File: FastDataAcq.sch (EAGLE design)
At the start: 229 parts, among them IC1 LT1963AEQ, IC2 FT230XQ, IC3 ADCMP553BRMZ, J1 USB_MICROAB_SMT, J2 MICRO-FIT_3.0_2POS_RA_SMD, X1 SMA-142-0701-801/806, X2 87832-14, X3 SMA-142-0701-801/806, Y1 SI530-500, Y2 DNP, Y3 100MHz

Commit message: Schematic fixes and beginning board layout
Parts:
- removed C105, C106, C107, C108, C109, C110, C111, C112: .1uF, Schuyler:CAPACITOR0204_REVERSE
- removed R40: 100 0.1%, rcl:R-US_R0402
- removed R41: 330, rcl:R-US_R0201
- added C16: .1uF, Schuyler:CAPACITOR0204_REVERSE
- added C66: 10pF, rcl:C-EUC0201
- added C67: 33uF, SparkFun-Passives:CAP0805
- added C69, C73: 22uF 150mOhm ESR, rcl:C-USC0805
- added C70, C72: 10uF, rcl:C-EUC0603
- added C75: NA, rcl:C-EUC0603
- C10, C11, C28, C29, C87: value 33uF -> .1uF; device SparkFun-Passives:CAP0805 -> Schuyler:CAPACITOR0204_REVERSE; PARTNUMBER 445-8238-1-ND -> 587-2152-1-ND; SUPPLIER (none) -> DIGIKEY
- C100: value .1uF -> 47pF; device Schuyler:CAPACITOR0204_REVERSE -> rcl:C-EUC0201; PARTNUMBER 587-2152-1-ND -> 445-1782-1-ND; SUPPLIER DIGIKEY -> (none)
- C101, C103: value .1uF -> 10nF; device Schuyler:CAPACITOR0204_REVERSE -> rcl:C-EUC0201; PARTNUMBER 587-2152-1-ND -> 445-1793-1-ND; SUPPLIER DIGIKEY -> (none)
- C102: value 4.7uF -> 1uF; device Schuyler:CAPACITOR0304_REVERSE -> Schuyler:CAPACITOR0204_REVERSE; PARTNUMBER 445-13745-1-ND -> 445-9091-1-ND
- C12, C13, C15, C17, C22: value 10uF -> .1uF; device rcl:C-EUC0603 -> Schuyler:CAPACITOR0204_REVERSE; PARTNUMBER 445-4112-1-ND -> 587-2152-1-ND
- C14, C25, C26, C27, C8, C9: value 10pF -> .1uF; device rcl:C-EUC0201 -> Schuyler:CAPACITOR0204_REVERSE; PARTNUMBER 445-1769-1-ND -> 587-2152-1-ND; SUPPLIER (none) -> DIGIKEY
- C18: value NA -> 10uF; PARTNUMBER (none) -> 445-4112-1-ND; SUPPLIER (none) -> DIGIKEY
- C2: value 10uF -> 10pF; device rcl:C-EUC0603 -> rcl:C-EUC0201; PARTNUMBER 445-4112-1-ND -> 445-1769-1-ND; SUPPLIER DIGIKEY -> (none)
- C20: value 10uF -> 100uF; device rcl:C-EUC0603 -> Schuyler:CAP_POL_D9_SERIES; MANPARTNUMBER (none) -> ECASD91B107M012K00; PARTNUMBER 445-4112-1-ND -> 490-5480-1-ND; SUPPLIER DIGIKEY -> (none)
- C23, C24: value 22uF 150mOhm ESR -> .1uF; device rcl:C-USC0805 -> Schuyler:CAPACITOR0204_REVERSE; PARTNUMBER P16231CT-ND -> 587-2152-1-ND
- C3: value 100uF -> 33uF; device Schuyler:CAP_POL_D9_SERIES -> SparkFun-Passives:CAP0805; MANPARTNUMBER ECASD91B107M012K00 -> (none); PARTNUMBER 490-5480-1-ND -> 445-8238-1-ND
- C30, C38: value 33uF -> 0.47uF; device SparkFun-Passives:CAP0805 -> Schuyler:CAPACITOR0204_REVERSE; PARTNUMBER 445-8238-1-ND -> 1276-1779-1-ND; SUPPLIER (none) -> DIGIKEY
- C31: value 22uF 150mOhm ESR -> 33uF; device rcl:C-USC0805 -> SparkFun-Passives:CAP0805; PARTNUMBER P16231CT-ND -> 445-8238-1-ND; SUPPLIER DIGIKEY -> (none)
- C32, C65, C68: value 4.7uF -> 10uF; device Schuyler:CAPACITOR0304_REVERSE -> rcl:C-EUC0603; PARTNUMBER 445-13745-1-ND -> 445-4112-1-ND
- C33, C71: value 4.7uF -> 10pF; device Schuyler:CAPACITOR0304_REVERSE -> rcl:C-EUC0201; PARTNUMBER 445-13745-1-ND -> 445-1769-1-ND; SUPPLIER DIGIKEY -> (none)
- C34, C74: value 4.7uF -> 33uF; device Schuyler:CAPACITOR0304_REVERSE -> SparkFun-Passives:CAP0805; PARTNUMBER 445-13745-1-ND -> 445-8238-1-ND; SUPPLIER DIGIKEY -> (none)
- C35, C40, C50: device Schuyler:CAPACITOR0304_REVERSE -> Schuyler:CAPACITOR; PARTNUMBER 445-13745-1-ND -> (none); SUPPLIER DIGIKEY -> (none)
- C36, C37, C41, C42, C45, C62: value 0.47uF -> 4.7uF; device Schuyler:CAPACITOR0304_REVERSE -> Schuyler:CAPACITOR; PARTNUMBER 445-13744-1-ND -> (none); SUPPLIER DIGIKEY -> (none)
- C39: value 33uF -> 4.7uF; device SparkFun-Passives:CAP0805 -> Schuyler:CAPACITOR; PARTNUMBER 445-8238-1-ND -> (none)
- C43, C44, C47, C93: value .1uF -> 4.7uF; device Schuyler:CAPACITOR0204_REVERSE -> Schuyler:CAPACITOR; PARTNUMBER 587-2152-1-ND -> (none); SUPPLIER DIGIKEY -> (none)
- C46, C48, C49: value .1uF -> 0.47uF; PARTNUMBER 587-2152-1-ND -> 1276-1779-1-ND
- C5: value NA -> 10pF; device rcl:C-EUC0603 -> rcl:C-EUC0201; PARTNUMBER (none) -> 445-1769-1-ND
- C51, C52, C60: value 4.7uF -> 0.47uF; device Schuyler:CAPACITOR0304_REVERSE -> Schuyler:CAPACITOR0204_REVERSE; PARTNUMBER 445-13745-1-ND -> 1276-1779-1-ND
- C53, C58: value .1uF -> 10uF; device Schuyler:CAPACITOR0204_REVERSE -> rcl:C-EUC0603; PARTNUMBER 587-2152-1-ND -> 445-4112-1-ND
- C54: value .1uF -> 10pF; device Schuyler:CAPACITOR0204_REVERSE -> rcl:C-EUC0201; PARTNUMBER 587-2152-1-ND -> 445-1769-1-ND; SUPPLIER DIGIKEY -> (none)
- C55: value 0.47uF -> 33uF; device Schuyler:CAPACITOR0304_REVERSE -> SparkFun-Passives:CAP0805; PARTNUMBER 445-13744-1-ND -> 445-8238-1-ND; SUPPLIER DIGIKEY -> (none)
- C56: value 0.47uF -> 10uF; device Schuyler:CAPACITOR0304_REVERSE -> rcl:C-EUC0603; PARTNUMBER 445-13744-1-ND -> 445-4112-1-ND
- C57: value 4.7uF -> 22uF 150mOhm ESR; device Schuyler:CAPACITOR0304_REVERSE -> rcl:C-USC0805; PARTNUMBER 445-13745-1-ND -> P16231CT-ND
- C59: value 10nF -> 4.7uF; device rcl:C-EUC0201 -> Schuyler:CAPACITOR; PARTNUMBER 445-1793-1-ND -> (none)
- C6: value 10uF -> 33uF; device rcl:C-EUC0603 -> SparkFun-Passives:CAP0805; PARTNUMBER 445-4112-1-ND -> 445-8238-1-ND; SUPPLIER DIGIKEY -> (none)
- C61: device Schuyler:CAPACITOR0304_REVERSE -> Schuyler:CAPACITOR0204_REVERSE; PARTNUMBER 445-13744-1-ND -> 1276-1779-1-ND
- C63: value 1uF -> 0.47uF; PARTNUMBER 445-9091-1-ND -> 1276-1779-1-ND
- C64: value 10nF -> 0.47uF; device rcl:C-EUC0201 -> Schuyler:CAPACITOR0204_REVERSE; PARTNUMBER 445-1793-1-ND -> 1276-1779-1-ND; SUPPLIER (none) -> DIGIKEY
- C7: value 10uF -> NA; PARTNUMBER 445-4112-1-ND -> (none); SUPPLIER DIGIKEY -> (none)
- C76: value 0.47uF -> 10nF; device Schuyler:CAPACITOR0304_REVERSE -> rcl:C-EUC0201; PARTNUMBER 445-13744-1-ND -> 445-1793-1-ND; SUPPLIER DIGIKEY -> (none)
- C77: value 100pF -> .1uF; device rcl:C-EUC0603 -> Schuyler:CAPACITOR0204_REVERSE; PARTNUMBER 1276-1295-1-ND -> 587-2152-1-ND
- C78: value .1uF -> 1uF; PARTNUMBER 587-2152-1-ND -> 445-9091-1-ND
- C79, C82: value .1uF -> 4.7nF; device Schuyler:CAPACITOR0204_REVERSE -> rcl:C-EUC0201; PARTNUMBER 587-2152-1-ND -> 445-1795-1-ND; SUPPLIER DIGIKEY -> (none)
- C80: value 4.7nF -> .1uF; device rcl:C-EUC0201 -> Schuyler:CAPACITOR0204_REVERSE; PARTNUMBER 445-1795-1-ND -> 587-2152-1-ND; SUPPLIER (none) -> DIGIKEY
- C81: value 4.7nF -> 1uF; device rcl:C-EUC0201 -> Schuyler:CAPACITOR0204_REVERSE; PARTNUMBER 445-1795-1-ND -> 445-9091-1-ND; SUPPLIER (none) -> DIGIKEY
- C84: value 33uF -> 10nF; device SparkFun-Passives:CAP0805 -> rcl:C-EUC0201; PARTNUMBER 445-8238-1-ND -> 445-1793-1-ND
- C86: value 1uF -> 10nF; device Schuyler:CAPACITOR0204_REVERSE -> rcl:C-EUC0201; PARTNUMBER 445-9091-1-ND -> 445-1793-1-ND; SUPPLIER DIGIKEY -> (none)
- C88: value 4.7uF -> 100pF; device Schuyler:CAPACITOR0304_REVERSE -> rcl:C-EUC0201; PARTNUMBER 445-13745-1-ND -> 445-4675-1-ND
- C90, C94: value 10nF -> .1uF; device rcl:C-EUC0201 -> Schuyler:CAPACITOR0204_REVERSE; PARTNUMBER 445-1793-1-ND -> 587-2152-1-ND; SUPPLIER (none) -> DIGIKEY
- C91: value .1uF -> 33uF; device Schuyler:CAPACITOR0204_REVERSE -> SparkFun-Passives:CAP0805; PARTNUMBER 587-2152-1-ND -> 445-8238-1-ND; SUPPLIER DIGIKEY -> (none)
- C92: value 10nF -> 4.7uF; device rcl:C-EUC0201 -> Schuyler:CAPACITOR0304_REVERSE; PARTNUMBER 445-1793-1-ND -> 445-13745-1-ND; SUPPLIER (none) -> DIGIKEY
- C96: value 47pF -> .1uF; device rcl:C-EUC0201 -> Schuyler:CAPACITOR0204_REVERSE; PARTNUMBER 445-1782-1-ND -> 587-2152-1-ND; SUPPLIER (none) -> DIGIKEY
- C98: value 47pF -> 33uF; device rcl:C-EUC0201 -> SparkFun-Passives:CAP0805; PARTNUMBER 445-1782-1-ND -> 445-8238-1-ND
- C99: value 1uF -> 47pF; device Schuyler:CAPACITOR0204_REVERSE -> rcl:C-EUC0201; PARTNUMBER 445-9091-1-ND -> 445-1782-1-ND; SUPPLIER DIGIKEY -> (none)
- D2: device Schuyler:LED_0603_GREEN -> Schuyler:LED_0603_BLUE
- D3: device Schuyler:LED_0603_BLUE -> Schuyler:LED_0603_GREEN
- D4: device Schuyler:LED_0603_BLUE -> Schuyler:LED_0603_RED
- D6: device Schuyler:LED_0603_RED -> Schuyler:LED_0603_BLUE
- J1: value USB_MICROAB_SMT -> MICRO-FIT_3.0_2POS_RA_SMD; device Schuyler:USB_MICROAB_SMT -> Schuyler:MICRO-FIT_3.0_2POS_RA_SMD
- J2: value MICRO-FIT_3.0_2POS_RA_SMD -> USB_MICROAB_SMT; device Schuyler:MICRO-FIT_3.0_2POS_RA_SMD -> Schuyler:USB_MICROAB_SMT
- JP2: value M10" -> (none); device SparkFun-Connectors:M10" -> SparkFun-Passives:JUMPER-2PTH
- JP3: value (none) -> M10"; device SparkFun-Passives:JUMPER-2PTH -> SparkFun-Connectors:M10"
- L10, L7, L9: value (none) -> 2.2uH; device Schuyler:FERRITE_BEADS_BLM18SG260 -> Schuyler:INDUCTOR_3X3.6; PARTNUMBER (none) -> 541-1322-1-ND; SUPPLIER (none) -> DIGIKEY
- L11: device Schuyler:FERRITE_BEADS_BLM18SG331 -> Schuyler:FERRITE_BEADS_BLM18SG260
- L12: value CHOKE_CM_ACM7060-301 -> (none); device Schuyler:CHOKE_CM_ACM7060-301 -> Schuyler:FERRITE_BEADS_BLM18SG260
- L13: device Schuyler:FERRITE_BEADS_BLM18SG260 -> Schuyler:FERRITE_BEADS_BLM18SG331
- L2: value 2.2uH -> CHOKE_CM_ACM7060-301; device Schuyler:INDUCTOR_3X3.6 -> Schuyler:CHOKE_CM_ACM7060-301; PARTNUMBER 541-1322-1-ND -> (none); SUPPLIER DIGIKEY -> (none)
- L4, L5: value 2.2uH -> (none); device Schuyler:INDUCTOR_3X3.6 -> Schuyler:FERRITE_BEADS_BLM18SG260; PARTNUMBER 541-1322-1-ND -> (none); SUPPLIER DIGIKEY -> (none)
- L6: value 2.2uH -> (none); device Schuyler:INDUCTOR_5.18X5.49 -> Schuyler:FERRITE_BEADS_BLM18SG260; PARTNUMBER 541-1220-1-ND -> (none); SUPPLIER DIGIKEY -> (none)
- L8: value (none) -> 2.2uH; device Schuyler:FERRITE_BEADS_BLM18SG260 -> Schuyler:INDUCTOR_5.18X5.49; PARTNUMBER (none) -> 541-1220-1-ND; SUPPLIER (none) -> DIGIKEY
- R1, R6: value NA -> 10k; device rcl:R-US_R0603 -> rcl:R-US_R0201; MANPARTNUMBER (none) -> RC0603J103CS; MANUFACTURER (none) -> Samsung Electro-Mechanics America, Inc; PARTNUMBER (none) -> 1276-3817-1-ND; SUPPLIER (none) -> DIGIKEY
- R10: value NA -> 210K; device rcl:R-US_R0603 -> rcl:R-US_R0201; PARTNUMBER (none) -> P210KABCT-ND; SUPPLIER (none) -> DIGIKEY
- R11: value 649K -> 422K; PARTNUMBER P649KABCT-ND -> P442KABCT-ND
- R12: value 150K -> 10k; MANPARTNUMBER (none) -> RC0603J103CS; MANUFACTURER (none) -> Samsung Electro-Mechanics America, Inc; PARTNUMBER 1276-3719-1-ND -> 1276-3817-1-ND
- R13: value NA -> 270k; device rcl:R-US_R0603 -> rcl:R-US_R0201; PARTNUMBER (none) -> P270KABCT-ND; SUPPLIER (none) -> DIGIKEY
- R14: value 523K -> 1k; PARTNUMBER P523KABCT-ND -> 1276-3797-1-ND
- R15: value 523K -> 845k; PARTNUMBER P523KABCT-ND -> P845KABCT-ND
- R16: value 523K -> 210K; PARTNUMBER P523KABCT-ND -> P210KABCT-ND
- R17: value 210K -> 270k; PARTNUMBER P210KABCT-ND -> P270KABCT-ND
- R18: value 150K -> 523K; PARTNUMBER 1276-3719-1-ND -> P523KABCT-ND
- R19: value 523K -> 806K; PARTNUMBER P523KABCT-ND -> P806KABCT-ND
- R20: value 280K -> 649K; PARTNUMBER P280KABCT-ND -> P649KABCT-ND
- R21: value 270k -> 523K; PARTNUMBER P270KABCT-ND -> P523KABCT-ND
- R22: value 210K -> 1.15k 1%; device rcl:R-US_R0201 -> rcl:R-US_R0603; MANPARTNUMBER (none) -> RC1608F1151CS; MANUFACTURER (none) -> Samsung Electro-Mechanics America, Inc; PARTNUMBER P210KABCT-ND -> 1276-4649-1-ND
- R23, R34, R4, R8: value 10k -> NA; device rcl:R-US_R0201 -> rcl:R-US_R0603; MANPARTNUMBER RC0603J103CS -> (none); MANUFACTURER Samsung Electro-Mechanics America, Inc -> (none); PARTNUMBER 1276-3817-1-ND -> (none); SUPPLIER DIGIKEY -> (none)
- R24: value 1k -> 280K; PARTNUMBER 1276-3797-1-ND -> P280KABCT-ND
- R25: value 210K -> 100; device rcl:R-US_R0201 -> rcl:R-US_R0603; MANPARTNUMBER (none) -> RC1608J101CS; MANUFACTURER (none) -> Samsung Electro-Mechanics America, Inc; PARTNUMBER P210KABCT-ND -> 1276-5038-1-ND
- R26: value 806K -> 2k 1%; device rcl:R-US_R0201 -> rcl:R-US_R0603; MANPARTNUMBER (none) -> RC1608F202CS; MANUFACTURER (none) -> Samsung Electro-Mechanics America, Inc; PARTNUMBER P806KABCT-ND -> 1276-3495-1-ND
- R27: value 845k -> 523K; PARTNUMBER P845KABCT-ND -> P523KABCT-ND
- R28: value 649K -> NA; device rcl:R-US_R0201 -> rcl:R-US_R0603; PARTNUMBER P649KABCT-ND -> (none); SUPPLIER DIGIKEY -> (none)
- R29: value 422K -> 210K; PARTNUMBER P442KABCT-ND -> P210KABCT-ND
- R30: value 270k -> 649K; PARTNUMBER P270KABCT-ND -> P649KABCT-ND
- R31: value 1.15k 1% -> 523K; device rcl:R-US_R0603 -> rcl:R-US_R0201; MANPARTNUMBER RC1608F1151CS -> (none); MANUFACTURER Samsung Electro-Mechanics America, Inc -> (none); PARTNUMBER 1276-4649-1-ND -> P523KABCT-ND
- R32: value 2k 1% -> 150K; device rcl:R-US_R0603 -> rcl:R-US_R0201; MANPARTNUMBER RC1608F202CS -> (none); MANUFACTURER Samsung Electro-Mechanics America, Inc -> (none); PARTNUMBER 1276-3495-1-ND -> 1276-3719-1-ND
- R33: value 50 -> 150K; MANPARTNUMBER RC0603F49R9C -> (none); MANUFACTURER Samsung Electro-Mechanics America, Inc -> (none); PARTNUMBER 1276-3590-1-ND -> 1276-3719-1-ND
- R35, R36: value 10k -> 100 0.1%; device rcl:R-US_R0201 -> rcl:R-US_R0402; MANPARTNUMBER RC0603J103CS -> ERA-2AEB101X; MANUFACTURER Samsung Electro-Mechanics America, Inc -> Panasonic Electronic Components; PARTNUMBER 1276-3817-1-ND -> P100DCCT-ND
- R37: value 10k -> 4.7k; MANPARTNUMBER RC0603J103CS -> ERJ-1GNJ472C; MANUFACTURER Samsung Electro-Mechanics America, Inc -> Panasonic Electronic Components; PARTNUMBER 1276-3817-1-ND -> P4.7AECT-ND
- R38: value NA -> 330; device rcl:R-US_R0603 -> rcl:R-US_R0201; MANPARTNUMBER (none) -> RC0603J331CS; MANUFACTURER (none) -> Samsung Electro-Mechanics America, Inc; PARTNUMBER (none) -> 1276-3787-1-ND; SUPPLIER (none) -> DIGIKEY
- R39: value 100 0.1% -> 0; device rcl:R-US_R0402 -> rcl:R-US_R0603; MANPARTNUMBER ERA-2AEB101X -> (none); MANUFACTURER Panasonic Electronic Components -> (none); PARTNUMBER P100DCCT-ND -> 311-0.0GRCT-ND
- R42: value 4.7k -> 330; MANPARTNUMBER ERJ-1GNJ472C -> RC0603J331CS; MANUFACTURER Panasonic Electronic Components -> Samsung Electro-Mechanics America, Inc; PARTNUMBER P4.7AECT-ND -> 1276-3787-1-ND
- R43: value 0 -> 330; device rcl:R-US_R0603 -> rcl:R-US_R0201; MANPARTNUMBER (none) -> RC0603J331CS; MANUFACTURER (none) -> Samsung Electro-Mechanics America, Inc; PARTNUMBER 311-0.0GRCT-ND -> 1276-3787-1-ND
- R46, R47: value 27 -> 330; MANPARTNUMBER (none) -> RC0603J331CS; MANUFACTURER (none) -> Samsung Electro-Mechanics America, Inc; PARTNUMBER 1276-3577-1-ND -> 1276-3787-1-ND
- R48: value 10k -> 330; device rcl:R-US_R0603 -> rcl:R-US_R0201; MANPARTNUMBER (none) -> RC0603J331CS; MANUFACTURER (none) -> Samsung Electro-Mechanics America, Inc; PARTNUMBER 311-0.0GRCT-ND -> 1276-3787-1-ND
- R49: value 26.1k -> 10k; device rcl:R-US_R0603 -> rcl:R-US_R0201; MANPARTNUMBER (none) -> RC0603J103CS; MANUFACTURER (none) -> Samsung Electro-Mechanics America, Inc; PARTNUMBER 311-0.0GRCT-ND -> 1276-3817-1-ND
- R50: device rcl:R-US_R0603 -> rcl:R-US_R0201; MANPARTNUMBER (none) -> RC0603J103CS; MANUFACTURER (none) -> Samsung Electro-Mechanics America, Inc; PARTNUMBER 311-0.0GRCT-ND -> 1276-3817-1-ND
- R51: value 16k -> 50; device rcl:R-US_R0603 -> rcl:R-US_R0201; MANPARTNUMBER (none) -> RC0603F49R9C; MANUFACTURER (none) -> Samsung Electro-Mechanics America, Inc; PARTNUMBER 311-0.0GRCT-ND -> 1276-3590-1-ND
- R52, R53: value 50 -> 27; MANPARTNUMBER RC0603F49R9C -> (none); MANUFACTURER Samsung Electro-Mechanics America, Inc -> (none); PARTNUMBER 1276-3590-1-ND -> 1276-3577-1-ND
- R54: value 50 -> 26.1k; device rcl:R-US_R0201 -> rcl:R-US_R0603; MANPARTNUMBER RC0603F49R9C -> (none); MANUFACTURER Samsung Electro-Mechanics America, Inc -> (none); PARTNUMBER 1276-3590-1-ND -> 311-0.0GRCT-ND
- R55: value 100 -> 16k; MANPARTNUMBER RC1608J101CS -> (none); MANUFACTURER Samsung Electro-Mechanics America, Inc -> (none); PARTNUMBER 1276-5038-1-ND -> 311-0.0GRCT-ND
- R56, R57: value 330 -> 10k; device rcl:R-US_R0201 -> rcl:R-US_R0603; MANPARTNUMBER RC0603J331CS -> (none); MANUFACTURER Samsung Electro-Mechanics America, Inc -> (none); PARTNUMBER 1276-3787-1-ND -> 311-0.0GRCT-ND
- R58: value 330 -> NA; device rcl:R-US_R0201 -> rcl:R-US_R0603; MANPARTNUMBER RC0603J331CS -> (none); MANUFACTURER Samsung Electro-Mechanics America, Inc -> (none); PARTNUMBER 1276-3787-1-ND -> 311-0.0GRCT-ND
- R59, R60: value 330 -> 50; MANPARTNUMBER RC0603J331CS -> RC0603F49R9C; PARTNUMBER 1276-3787-1-ND -> 1276-3590-1-ND
- R62: value NA -> 50; device rcl:R-US_R0603 -> rcl:R-US_R0201; MANPARTNUMBER (none) -> RC0603F49R9C; MANUFACTURER (none) -> Samsung Electro-Mechanics America, Inc; PARTNUMBER 311-0.0GRCT-ND -> 1276-3590-1-ND
- R7: value 3.3k 0.1% -> 4.7k; device rcl:R-US_R0603 -> rcl:R-US_R0201; MANPARTNUMBER (none) -> ERJ-1GNJ472C; MANUFACTURER (none) -> Panasonic Electronic Components; PARTNUMBER P3.3KDBCT-ND -> P4.7AECT-ND
- R9: value 4.7k -> 3.3k 0.1%; device rcl:R-US_R0201 -> rcl:R-US_R0603; MANPARTNUMBER ERJ-1GNJ472C -> (none); MANUFACTURER Panasonic Electronic Components -> (none); PARTNUMBER P4.7AECT-ND -> P3.3KDBCT-ND
- U$10: value XCFXXS04 -> LMH6555; device Schuyler:XCFXXS04 -> Schuyler:LMH6555
- U$11: value SLIDER_SPDT_1101M2S3AQE2 -> LMV321SC-70; device Schuyler:SLIDER_SPDT_1101M2S3AQE2 -> Schuyler:LMV321SC-70
- U$3: value LTC3374QFN -> SLIDER_SPDT_1101M2S3AQE2; device Schuyler:LTC3374QFN -> Schuyler:SLIDER_SPDT_1101M2S3AQE2
- U$4: value LT1963AEST-2.5 -> LTC3374QFN; device Schuyler:LT1963AEST-2.5 -> Schuyler:LTC3374QFN
- U$5: value LT1963AEST-3.3 -> LT1963AEST-2.5; device Schuyler:LT1963AEST-3.3 -> Schuyler:LT1963AEST-2.5
- U$6: value TMP421 -> LT1963AEST-3.3; device Schuyler:TMP421 -> Schuyler:LT1963AEST-3.3
- U$7: value LMH6555 -> XCFXXS04; device Schuyler:LMH6555 -> Schuyler:XCFXXS04
- U$8: value LMV321SC-70 -> TMP421; device Schuyler:LMV321SC-70 -> Schuyler:TMP421
- X1: value SMA-142-0701-801/806 -> 87832-14; device con-coax:SMA-142-0701-801/806 -> con-molex:87832-14; MANPARTNUMBER 142-0701-801 -> (none); MANUFACTURER Emerson Network Power Connectivity Johnson -> (none); PARTNUMBER J502-ND -> 57J0374; SUPPLIER DIGIKEY -> Newark
- X2: value 87832-14 -> SMA-142-0701-801/806; device con-molex:87832-14 -> con-coax:SMA-142-0701-801/806; MANPARTNUMBER (none) -> 142-0701-801; MANUFACTURER (none) -> Emerson Network Power Connectivity Johnson; PARTNUMBER 57J0374 -> J502-ND; SUPPLIER Newark -> DIGIKEY
- Y2: value DNP -> 100MHz; device Schuyler:SI500S -> Schuyler:DS1088L_100MHZ
- Y3: value 100MHz -> DNP; device Schuyler:DS1088L_100MHZ -> Schuyler:SI500S
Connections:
- removed net 1V9F: C33.1, C36.1, C41.1, C50.1, C51.1, C55.1, C56.1, C61.1, C62.1
- net !RXLED: now also D5.CATHODE; no longer D2.CATHODE
- net !TXLED: now also D6.CATHODE; no longer D3.CATHODE
- net 1V2: now also C2.1, C3.1, C36.1, C37.1, C38.1, L1.P$2, R10.2, R13.1, TP1.TP, U$2.VCCINT@1, U$2.VCCINT@2; no longer C25.1, C28.1, C32.1, C40.1, C45.1, L4.P$2, R21.1, R25.2, TP2.TP
- net 1V8: now also C33.1, C34.1, C47.1, C48.1, C49.1, C50.1, C51.1, C52.1, C62.1, C63.1, C64.1, L7.P$2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; no longer C26.1, C29.1, L5.P$2, R26.2, TP4.TP, U$2.GND@7
- net 1V9: now also C57.1, L4.P$1, L6.P$1, R22.2, R25.2; no longer C31.1, L7.P$1, L8.P$1, R31.2, R55.2
- net 1V9A: now also C10.2, C11.1, C12.1, C13.2, C14.1, C15.1, C16.2, C17.1, C19.1, C8.1, C9.2, L4.P$2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; no longer C103.1, C104.1, C105.1, C106.1, C107.1, C108.1, C109.1, C110.1, C111.1, C112.1, C38.1, L7.P$2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
- net 1V9D: now also C22.1, C23.1, C24.1, C25.1, C26.1, C27.1, C28.1, C29.1, C30.1, C31.1, L6.P$2; no longer C39.1, C43.1, C44.1, C46.1, C47.1, C48.1, C49.1, C53.1, C54.1, C58.1, L8.P$2
- net 2V3_1V9PRE: now also C54.1, C55.1, C56.1, L8.P$2, R21.2, TP6.TP; no longer C14.1, C19.1, C22.1, L3.P$2, R19.2, TP3.TP
- net 2V5: now also C69.1, L11.P$2, TP9.TP, U$5.OUT; no longer C23.1, L10.P$2, TP8.TP, U$4.OUT
- net 2V5A: now also C76.1, C77.1, C78.1, L11.P$1; no longer C64.1, C85.1, C86.1, L10.P$1
- net 2V8_2V5PRE: now also C66.1, C67.1, C68.1, L9.P$2, R27.2, R30.1, TP8.TP, U$5.IN; no longer C10.1, C20.1, C8.1, L1.P$2, R11.1, R15.2, TP1.TP, U$4.IN
- net 3V3: now also C102.1, C103.1, C39.1, C40.1, C41.1, C43.1, C44.1, C45.1, C46.1, C5.1, C6.1, C61.1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; no longer C27.1, C30.1, C34.1, C37.1, C52.1, C57.1, C63.1, C65.1, C68.1, C71.1, C74.1, C76.1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
- net 3V3A: now also C73.1, L12.P$2, TP10.TP, U$6.OUT; no longer C24.1, L9.P$2, TP9.TP, U$5.OUT
- net 3V3S: now also C104.1, C89.1, C90.1, C91.1, L12.P$1, U$10.VCC@1, U$10.VCC@2, U$10.VCC@3, U$11.V+; no longer C78.1, C79.1, C82.1, C84.1, L9.P$1, U$7.VCC@1, U$7.VCC@2, U$7.VCC@3, U$8.V+
- net 3V6_PRE3V3: now also C71.1, C72.1, C74.1, L10.P$2, R31.2, TP11.TP, U$6.IN; no longer C11.1, C21.1, C9.1, L2.P$2, R16.2, TP5.TP, U$5.IN
- net 5VUSB: now also C92.1, C97.2, L13.P$2; no longer C101.2, C102.1, L11.P$2
- net 5VUSB_CON: now also C101.1, J2.VCC, L13.P$1; no longer C95.1, J1.VCC, L11.P$1
- net ADC_CAL: now also R6.2; no longer R5.2
- net ADC_CALDLY/DES/!SCS: now also R1.1; no longer R8.1
- net ADC_CLK+: now also C79.2; no longer C80.2
- net ADC_CLK-: now also C82.2; no longer C81.2
- net ADC_DCLKRST: now also R4.2; no longer R3.2
- net ADC_FSR/ECE: now also R2.1, R3.2; no longer R1.1, R2.2
- net ADC_PD: now also R5.2; no longer R4.2
- net ADC_PWR_EN: now also R23.2, U$4G$5.EN; no longer R13.2, U$3G$5.EN
- net ADC_REXT: now also R9.2; no longer R7.2
- net ADC_TDIODE+: now also C88.1, U$8.DXP; no longer C77.1, U$6.DXP
- net ADC_TDIODE-: now also C88.2, U$8.DXN; no longer C77.2, U$6.DXN
- net ADC_VBG: now also R8.1; no longer R6.1
- net ADC_VCMO: now also U$11.+IN; no longer U$8.+IN
- net ADC_VCMO_BUFFER: now also U$10.VCM, U$11.-IN, U$11.VOUT; no longer U$7.VCM, U$8.-IN, U$8.VOUT
- net ADC_VINI+: now also U$10.VOUT+; no longer U$7.VOUT+
- net ADC_VINI-: now also U$10.VOUT-; no longer U$7.VOUT-
- net AGND: now also C10.1, C11.2, C12.2, C13.1, C14.2, C15.2, C16.1, C17.2, C19.2, C76.2, C77.2, C8.2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; no longer C103.2, C105.2, C106.2, C107.2, C108.2, C109.2, C110.2, C111.2, C112.2, C38.2, C64.2, C79.2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
- net ANALOG_PWR_EN: now also R28.2, U$4G$8.EN; no longer R10.2, U$3G$8.EN
- net CLK500+: now also C82.1; no longer C81.1
- net CLK500-: now also C79.1; no longer C80.1
- net DGND: now also C101.2, C103.2, C20.NEG, C25.2, C26.2, C27.2, C3.2, C38.2, C64.2, C67.2, C69.2, C70.2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; no longer C10.2, C101.1, C11.2, C12.2, C13.2, C15.2, C17.2, C19.2, C2.2, C20.2, C3.NEG, C30.2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
- net FPGA_CCLK: now also R34.1, R35.1, R36.2, U$7.CLK; no longer R38.1, R39.1, R40.2, U$10.CLK
- net FPGA_CLK1: now also Y2.OUT; no longer Y3.OUT
- net FPGA_CLK2: now also Y3.OUTPUT; no longer Y2.OUTPUT
- net FPGA_DIN: now also U$7.DO; no longer U$10.DO
- net FPGA_DONE: now also R38.1, TP13.TP, U$7.!CE; no longer R41.1, TP12.TP, U$10.!CE
- net FPGA_GPIO0: now also JP3.1; no longer JP2.1
- net FPGA_GPIO1: now also JP3.2; no longer JP2.2
- net FPGA_GPIO2: now also JP3.3; no longer JP2.3
- net FPGA_GPIO3: now also JP3.4; no longer JP2.4
- net FPGA_GPIO4: now also JP3.5; no longer JP2.5
- net FPGA_GPIO5: now also D4.CATHODE, JP3.6; no longer D6.CATHODE, JP2.6
- net FPGA_GPIO6: now also D3.CATHODE, JP3.7; no longer D5.CATHODE, JP2.7
- net FPGA_GPIO7: now also D2.CATHODE, JP3.8; no longer D4.CATHODE, JP2.8
- net FPGA_INITB: now also TP12.TP, U$7.OE/!RST; no longer TP13.TP, U$10.OE/!RST
- net FPGA_PROGRAMB: now also R39.2, R7.1; no longer R43.2, R9.1
- net FPGA_RXD: now also R47.2; no longer R44.2
- net FPGA_SCL: now also R50.1, U$8.SCL; no longer R36.1, U$6.SCL
- net FPGA_SDA: now also R49.1, U$8.SDA; no longer R35.1, R37.1, U$6.SDA
- net FPGA_TCK: now also U$7.TCK, X1.6; no longer U$10.TCK, X2.6
- net FPGA_TDI: now also X1.10; no longer X2.10
- net FPGA_TDO: now also U$7.TDI; no longer U$10.TDI
- net FPGA_TMS: now also U$7.TMS, X1.4; no longer U$10.TMS, X2.4
- net FPGA_TRIG+: now also R57.2, R61.2; no longer R48.2, R53.2
- net FPGA_TRIG-: now also R56.2, R60.2; no longer R50.2, R52.2
- net FPGA_TXD: now also R48.2; no longer R45.2
- net FTDI_RXD: now also R48.1; no longer R45.1
- net FTDI_TXD: now also R47.1; no longer R44.1
- net N$1: now also JP1.2, L2.P$4, U$3.P$1; no longer JP3.2, L12.P$4, U$11.P$1
- net N$10: now also D5.ANODE, R45.2; no longer D2.ANODE, R56.2
- net N$11: now also R39.1, U$7.!CF; no longer R43.1, U$10.!CF
- net N$12: now also C7.1, R13.2, R16.2, U$4G$1.EN; no longer C18.1, R21.2, R22.2, U$3G$1.EN
- net N$13: now also D6.ANODE, R46.2; no longer D3.ANODE, R57.2
- net N$14: now also R22.1, R26.2; no longer R31.1, R32.2
- net N$15: now also R54.2, R57.1; no longer R48.1, R49.2
- net N$16: now also C75.1, R30.2, R32.1, U$4G$3.EN; no longer C5.1, R11.2, R12.1, U$3G$3.EN
- net N$17: now also C20.POS, JP1.1, L5.P$1, R14.2, U$3.P$2; no longer C3.POS, JP3.1, L13.P$1, R24.2, U$11.P$2
- net N$18: now also R60.1, R61.1, R62.2; no longer R52.1, R53.1, R54.2
- net N$19: now also D4.ANODE, R44.2; no longer D6.ANODE, R60.2
- net N$2: now also R51.2, U$10.VIN-; no longer R33.2, U$7.VIN-
- net N$20: now also R55.2, R56.1; no longer R50.1, R51.2
- net N$21: now also D3.ANODE, R43.2; no longer D5.ANODE, R59.2
- net N$22: now also D2.ANODE, R42.2; no longer D4.ANODE, R58.2
- net N$26: no longer U$2.GND@8
- net N$3: now also R52.2; no longer R46.2
- net N$4: now also C99.2, J2.D+, R52.1; no longer C96.2, J1.D+, R46.1
- net N$5: now also C100.2, J2.D-, R53.1; no longer C98.2, J1.D-, R47.1
- net N$6: now also JP2.1, R18.2, U$4G$9.MODE; no longer JP1.1, R14.2, U$3G$9.MODE
- net N$7: now also R53.2; no longer R47.2
- net N$8: now also C96.2, R45.1, R46.1; no longer C100.2, R56.1, R57.1
- net N$9: now also R14.1; no longer R24.1
- net PGOOD: now also R12.1, TP2.TP, U$4G$9.PGOOD_ALL; no longer R23.1, TP11.TP, U$3G$9.PGOOD_ALL
- net POWER_IN+: now also J1.P$2, L2.P$1; no longer J2.P$2, L12.P$1
- net POWER_IN-: now also J1.P$1, L2.P$2; no longer J2.P$1, L12.P$2
- net PROM_TDO: now also U$7.TDO, X1.8; no longer U$10.TDO, X2.8
- net S1FB: now also C5.2, R15.1, R17.2, U$4G$1.FB; no longer C27.2, R27.1, R30.2, U$3G$1.FB
- net S1SW: now also L3.P$1, U$4G$1.SW, U$4G$2.SW; no longer L6.P$1, U$3G$1.SW, U$3G$2.SW
- net S3FB: now also C71.2, R31.1, R33.2, U$4G$3.FB; no longer C9.2, R16.1, R18.2, U$3G$3.FB
- net S3SW: now also L10.P$1, U$4G$3.SW; no longer L2.P$1, U$3G$3.SW
- net S4FB: now also C33.2, R19.1, R20.2, U$4G$4.FB; no longer C26.2, R26.1, R28.2, U$3G$4.FB
- net S4SW: now also L7.P$1, U$4G$4.SW; no longer L5.P$1, U$3G$4.SW
- net S5FB: now also C54.2, R21.1, R24.2, U$4G$5.FB; no longer C14.2, R19.1, R20.2, U$3G$5.FB
- net S5SW: now also L8.P$1, U$4G$5.SW, U$4G$6.SW; no longer L3.P$1, U$3G$5.SW, U$3G$6.SW
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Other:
- note removed: "TODO: Change 0.1uF 4V capacitors to 6V"
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
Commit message: Board layout in progress. Other minor fixes.
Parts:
- removed C30: 0.47uF, Schuyler:CAPACITOR0204_REVERSE
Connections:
- removed net VCC: JP2.2
- net 1V9D: no longer C30.1
- net 3V3: now also R12.2, R37.2
- net FPGA_INITB: now also R37.1
- net VIN: now also JP2.2
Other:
- moved on the sheet: C4

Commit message: Minor schematic fixes, major PCB layout changes
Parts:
- removed R58: NA, rcl:R-US_R0603
- D1, D4: value (none) -> LED_0603_RED
- D2, D6: value (none) -> LED_0603_BLUE
- D3, D5: value (none) -> LED_0603_GREEN
- JP1, JP2: value (none) -> JUMPER-2PTH
- L11, L12, L4, L5, L6: value (none) -> 26
- L13: value (none) -> 330
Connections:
- net N$8 renamed 3V3OUT
- removed net AGND: C10.1, C104.2, C11.2, C12.2, C13.1, C14.2, C15.2, C16.1, C17.2, C19.2, C76.2, C77.2, C78.2, C8.2, C89.2, C9.1, C90.2, C91.2, R3.1, R4.1, R51.1, R9.1, U$1.GND@1, U$1.GND@2, U$1.GND@3, U$1.GND@4, U$1.GND@5, U$1.GND@6, U$1.GND@7, U$1.GND@8, U$1.GND_PAD, U$10.GND@1, U$10.GND@2, U$10.GND@3, U$10.GND@4, U$10.GND@5, U$10.GND@6, U$10.GND@7, U$10.GND@8, U$10.XPAD, U$11.V-, X2.2, Y1.GND
- removed net DGND: C1.2, C100.1, C101.2, C102.2, C103.2, C18.2, C20.NEG, C21.2, C22.2, C23.2, C24.2, C25.2, C26.2, C27.2, C28.2, C29.2, C3.2, C31.2, C32.2, C34.2, C35.2, C36.2, C37.2, C38.2, C39.2, C4.2, C40.2, C41.2, C42.2, C43.2, C44.2, C45.2, C46.2, C47.2, C48.2, C49.2, C50.2, C51.2, C52.2, C53.2, C55.2, C56.2, C57.2, C58.2, C59.2, C6.2, C60.2, C61.2, C62.2, C63.2, C64.2, C65.2, C67.2, C68.2, C69.2, C7.2, C70.2, C72.2, C73.2, C74.2, C75.2, C80.2, C81.2, C83.2, C84.2, C85.2, C86.2, C87.2, C92.2, C93.2, C94.2, C95.2, C96.1, C97.1, C98.2, C99.1, D1.CATHODE, IC1.GND, IC1.GND@1, IC2.GND, IC3.GND, J2.GND, JP3.9, L2.P$3, R11.1, R16.1, R17.1, R18.1, R20.1, R23.1, R24.1, R25.1, R26.1, R28.1, R29.1, R32.2, R33.1, R36.1, R58.2, R59.1, R62.1, U$1.DR_GND@1, U$1.DR_GND@2, U$1.DR_GND@3, U$1.DR_GND@4, U$1.DR_GND@5, U$1.DR_GND@6, U$1.DR_GND@7, U$1.DR_GND@8, U$2.GND@1, U$2.GND@11, U$2.GND@12, U$2.GND@13, U$2.GND@2, U$2.GND@3, U$2.GND@4, U$2.GND@5, U$2.GND@6, U$2.GND@7, U$2.GND@8, U$2.IO_L13P_M1_2, U$2.SUSPEND, U$4G$2.EN, U$4G$6.EN, U$4G$9.GND, U$4G$9.SYNC, U$5.GND@1, U$5.GND@2, U$6.GND@1, U$6.GND@2, U$7.GND, U$8.A0, U$8.A1, U$8.GND, U$9.ADR0, U$9.GND, X1.1, X1.11, X1.13, X1.3, X1.5, X1.7, X1.9, X3.2, Y2.GND@1, Y2.GND@2, Y3.GDN
- removed net FPGA_GPIO0: JP3.1, U$2.IO_L49P_D3_2
- removed net FPGA_SDL: U$2.IO_L62P_D5_2
- removed net N$26: U$2.GND@10, U$2.GND@9
- new net GND: C1.2, C10.1, C100.1, C101.2, C102.2, C103.2, C104.2, C11.2, C12.2, C13.1, C14.2, C15.2, C16.1, C17.2, C18.2, C19.2, C20.NEG, C21.2, C22.2, C23.2, C24.2, C25.2, C26.2, C27.2, C28.2, C29.2, C3.2, C31.2, C32.2, C34.2, C35.2, C36.2, C37.2, C38.2, C39.2, C4.2, C40.2, C41.2, C42.2, C43.2, C44.2, C45.2, C46.2, C47.2, C48.2, C49.2, C50.2, C51.2, C52.2, C53.2, C55.2, C56.2, C57.2, C58.2, C59.2, C6.2, C60.2, C61.2, C62.2, C63.2, C64.2, C65.2, C67.2, C68.2, C69.2, C7.2, C70.2, C72.2, C73.2, C74.2, C75.2, C76.2, C77.2, C78.2, C8.2, C80.2, C81.2, C83.2, C84.2, C85.2, C86.2, C87.2, C89.2, C9.1, C90.2, C91.2, C92.2, C93.2, C94.2, C95.2, C96.1, C97.1, C98.2, C99.1, D1.CATHODE, IC1.GND, IC1.GND@1, IC2.GND, IC2.GND@1, IC3.GND, J2.GND, JP3.9, L2.P$3, R11.1, R16.1, R17.1, R18.1, R20.1, R23.1, R24.1, R25.1, R26.1, R28.1, R29.1, R3.1, R32.2, R33.1, R36.1, R4.1, R51.1, R59.1, R62.1, R9.1, U$1.DR_GND@1, U$1.DR_GND@2, U$1.DR_GND@3, U$1.DR_GND@4, U$1.DR_GND@5, U$1.DR_GND@6, U$1.DR_GND@7, U$1.DR_GND@8, U$1.GND@1, U$1.GND@2, U$1.GND@3, U$1.GND@4, U$1.GND@5, U$1.GND@6, U$1.GND@7, U$1.GND@8, U$1.GND_PAD, U$10.GND@1, U$10.GND@2, U$10.GND@3, U$10.GND@4, U$10.GND@5, U$10.GND@6, U$10.GND@7, U$10.GND@8, U$10.XPAD, U$11.V-, U$2.GND@1, U$2.GND@10, U$2.GND@11, U$2.GND@12, U$2.GND@13, U$2.GND@2, U$2.GND@3, U$2.GND@4, U$2.GND@5, U$2.GND@6, U$2.GND@7, U$2.GND@8, U$2.GND@9, U$2.IO_L13P_M1_2, U$2.SUSPEND, U$4G$2.EN, U$4G$6.EN, U$4G$9.GND, U$4G$9.SYNC, U$5.GND@1, U$5.GND@2, U$6.GND@1, U$6.GND@2, U$7.GND, U$8.A0, U$8.A1, U$8.GND, U$9.ADR0, U$9.GND, X1.1, X1.11, X1.13, X1.3, X1.5, X1.7, X1.9, X2.2, X3.2, Y1.GND, Y2.GND@1, Y2.GND@2, Y3.GND
- net 1V8: now also R12.2
- net 3V3: no longer R12.2
- net FPGA_SDA: now also U$2.IO_L62P_D5_2
- net PGOOD: now also U$2.IO_L1P_3; no longer U$2.IO_L49N_D4_2
- net TRIG_REF: no longer R58.1
- net TRIG_RESET_HIGH: now also U$2.IO_L49P_D3_2
- net TRIG_RESET_LOW: now also U$2.IO_L49N_D4_2
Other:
- note added: "ADC and FPGA Connections"
- note removed: "ADC and FGPA Connections"

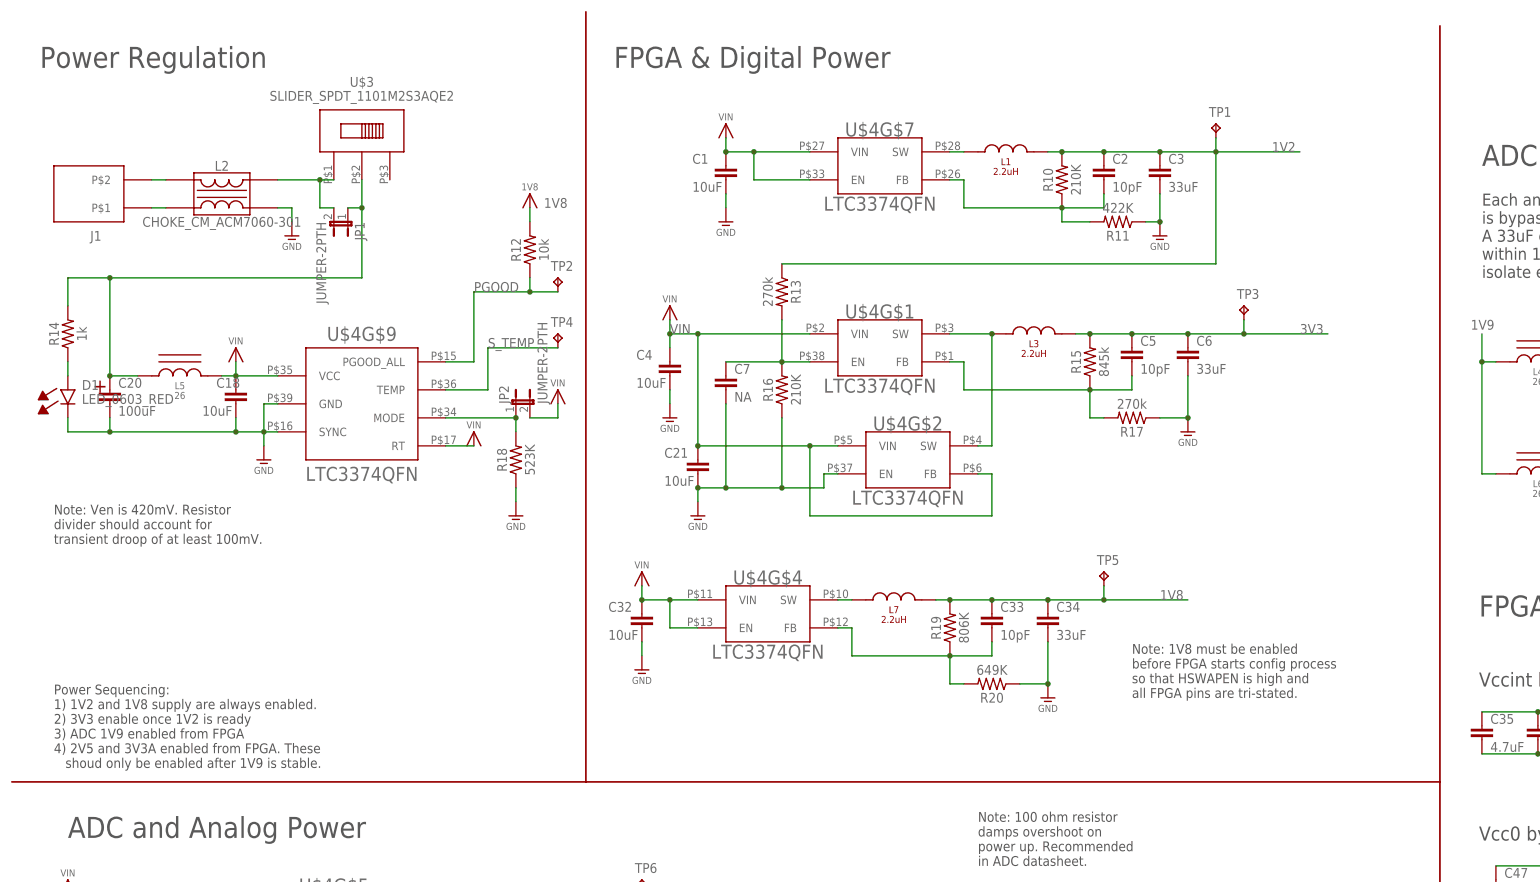
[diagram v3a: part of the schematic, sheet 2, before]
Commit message: New power switch layout
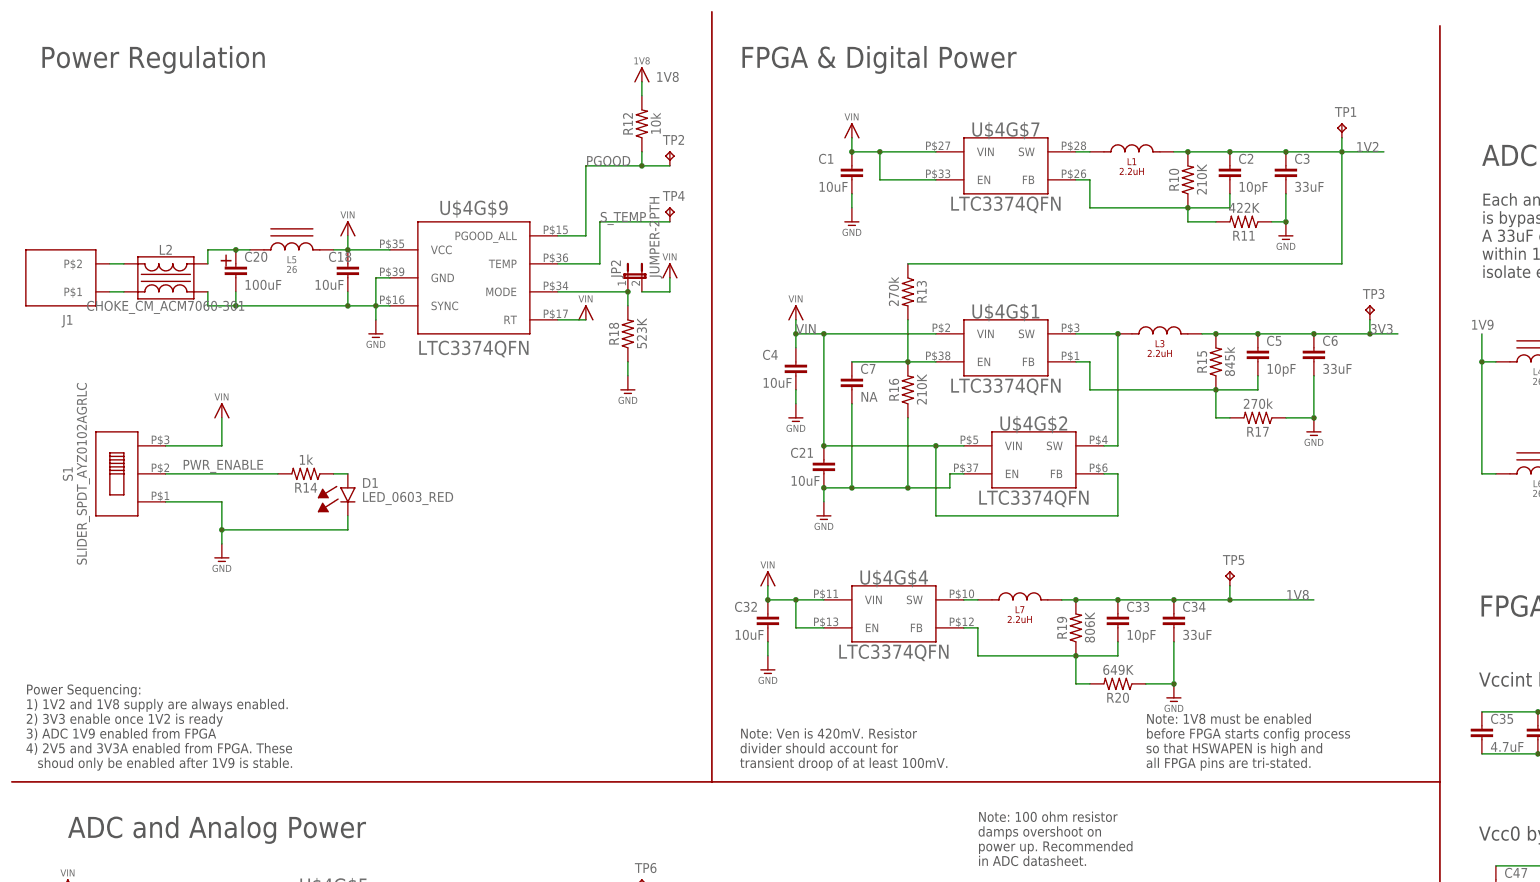
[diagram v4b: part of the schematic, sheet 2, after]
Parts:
- removed JP1: JUMPER-2PTH, SparkFun-Passives:JUMPER-2PTH
- removed U$3: SLIDER_SPDT_1101M2S3AQE2, Schuyler:SLIDER_SPDT_1101M2S3AQE2
- added S1: SLIDER_SPDT_AYZ0102AGRLC, Schuyler:SLIDER_SPDT_AYZ0102AGRLC
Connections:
- removed net N$1: JP1.2, L2.P$4, U$3.P$1
- removed net N$17: C20.POS, JP1.1, L5.P$1, R14.2, U$3.P$2
- new net N$24: C20.POS, L2.P$4, L5.P$1
- new net PWR_ENABLE: R14.2, S1.P$2
- net GND: now also S1.P$1
- net VIN: now also S1.P$3
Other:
- moved on the sheet: C1, C18, C2, C20, C21, C3, C32, C33, C34, C4, C5, C6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

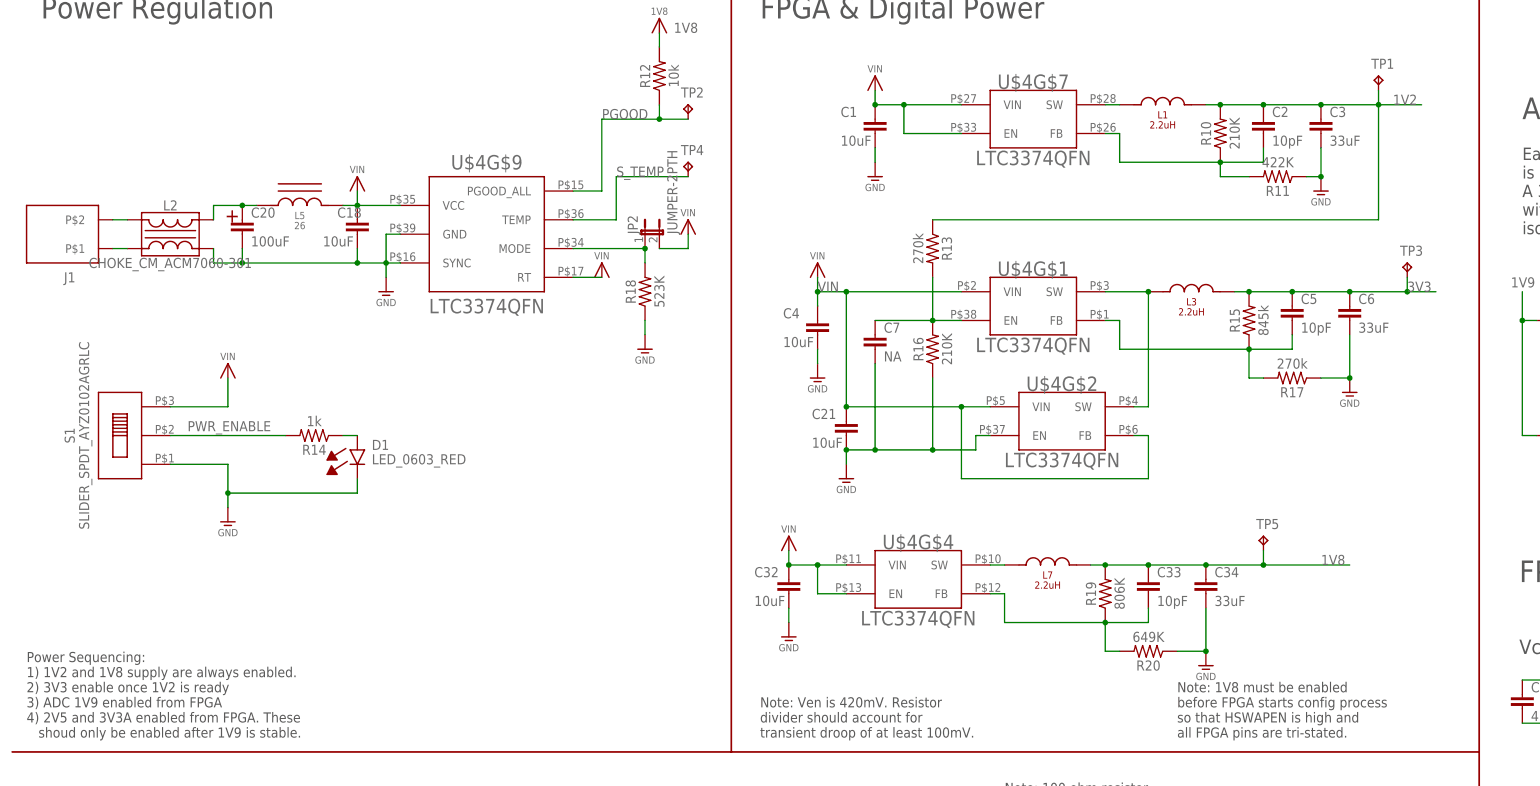
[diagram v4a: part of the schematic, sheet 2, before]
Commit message: Component placement semi-finalized
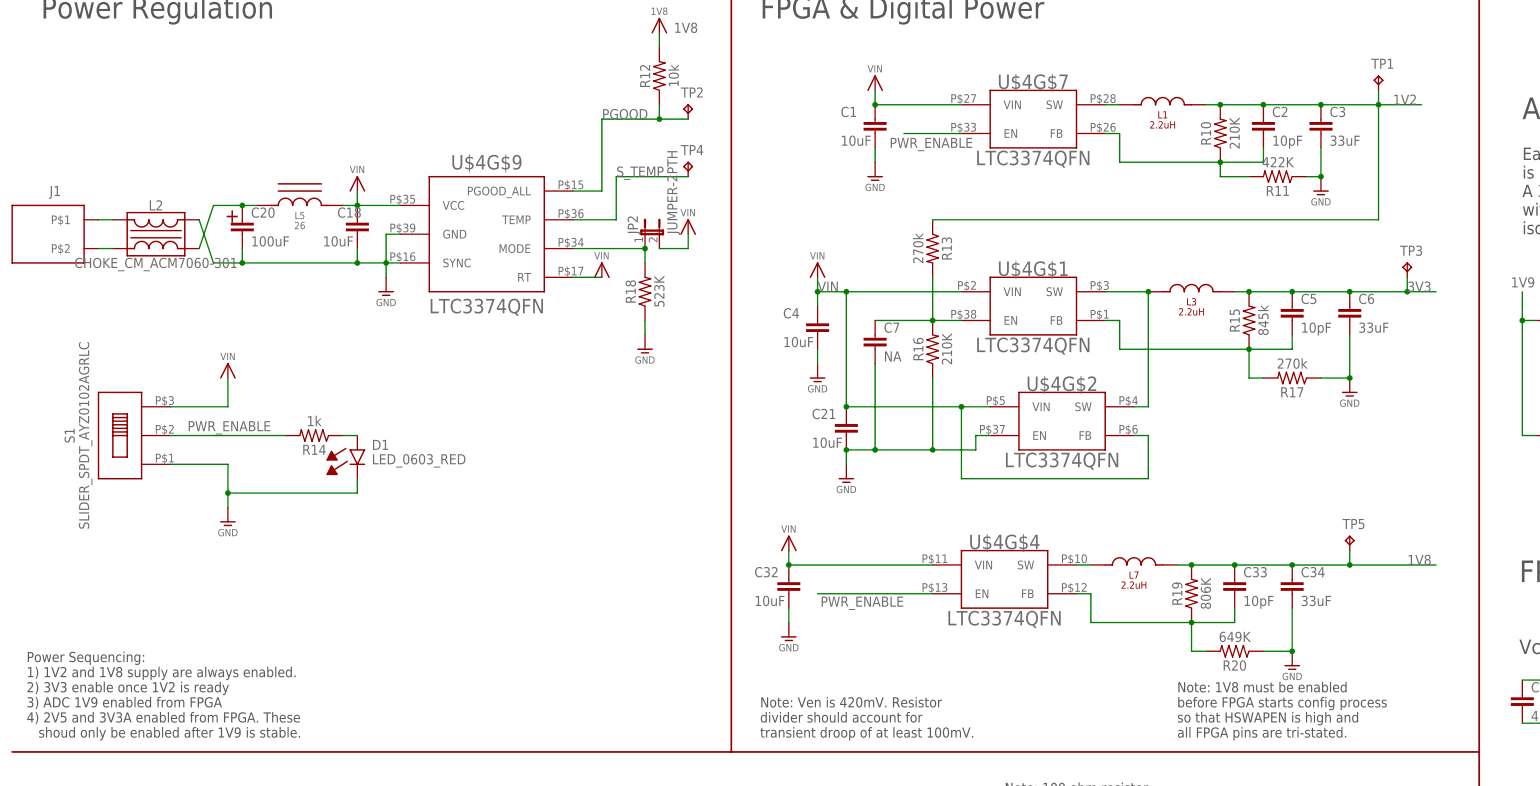
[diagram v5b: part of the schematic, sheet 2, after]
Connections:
- net N$12 renamed S1EN
- net N$16 renamed S4EN
- removed net POWER_IN+: J1.P$2, L2.P$1
- removed net POWER_IN-: J1.P$1, L2.P$2
- new net N$34: J1.P$1, L2.P$1
- new net N$35: J1.P$2, L2.P$2
- net GND: now also L2.P$4; no longer L2.P$3
- net N$24: now also L2.P$3; no longer L2.P$4
- net PWR_ENABLE: now also U$4G$4.EN, U$4G$7.EN
- net VIN: no longer U$4G$4.EN, U$4G$7.EN
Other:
- moved on the sheet: C33, C34, J1, L2, L7, R19, R20, TP5, U$4G$4
